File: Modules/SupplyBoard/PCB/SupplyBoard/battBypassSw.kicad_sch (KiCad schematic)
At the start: 0 parts

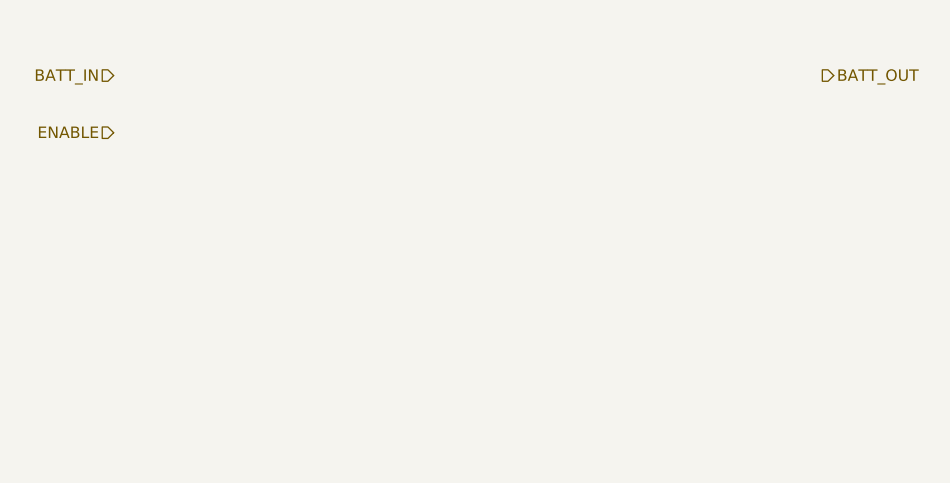
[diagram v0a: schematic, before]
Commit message: Supply board schematic and PCB
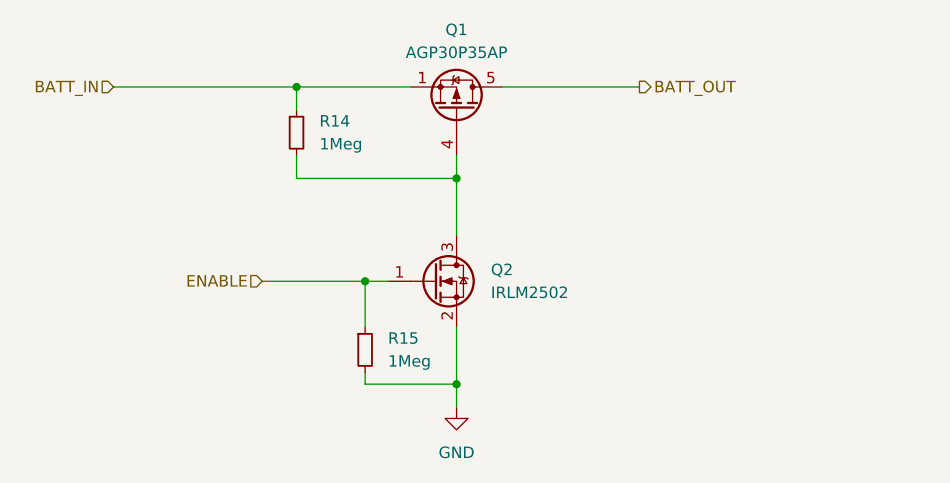
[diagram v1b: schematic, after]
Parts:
- added Q1: AGP30P35AP, Package_SON:Diodes_PowerDI3333-8, symbol Transistor_FET:DMP3013SFV
- added Q2: IRLM2502, Package_TO_SOT_SMD:SOT-23, symbol IcaroLib:IRLM2502
- added R14, R15: 1Meg, Resistor_SMD:R_0603_1608Metric_Pad0.98x0.95mm_HandSolder, symbol Device:R_Small
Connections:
- net BATT_IN: now also Q1.1 (S), Q1.2 (S), Q1.3 (S), R14.1
- net BATT_OUT: now also Q1.5 (D)
- net ENABLE: now also Q2.1 (G), R15.1
- new net: Q1.4 (G), Q2.3 (D), R14.2
- new net GND: Q2.2 (S), R15.2
